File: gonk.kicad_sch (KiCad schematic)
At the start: 10 parts

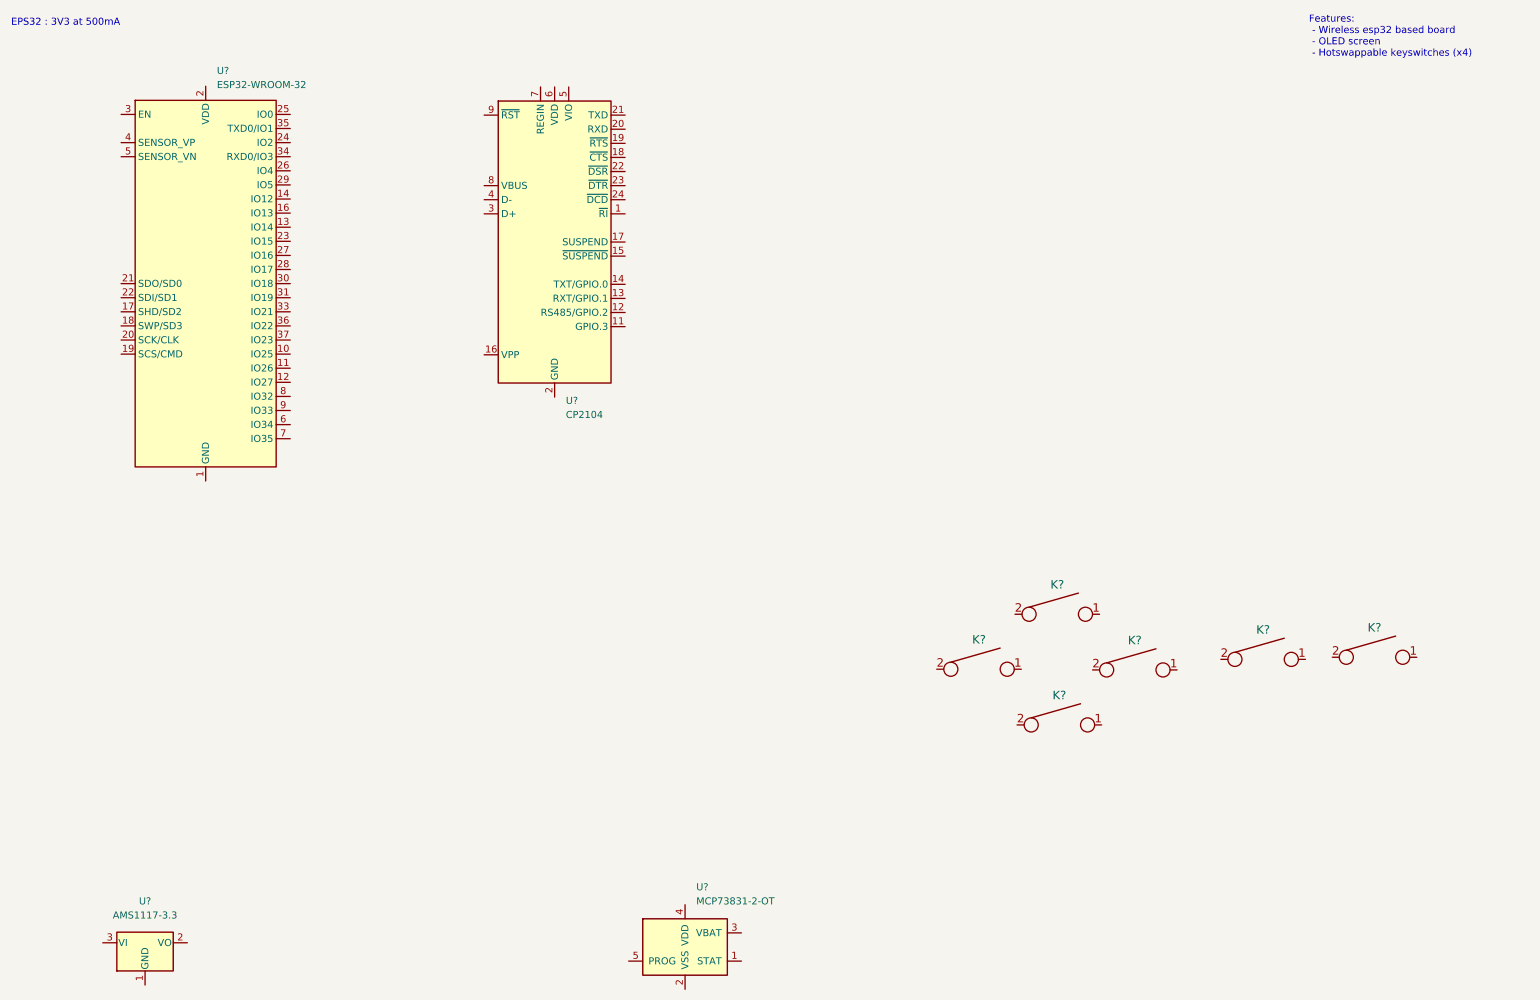
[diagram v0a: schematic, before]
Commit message: Added heiarchical
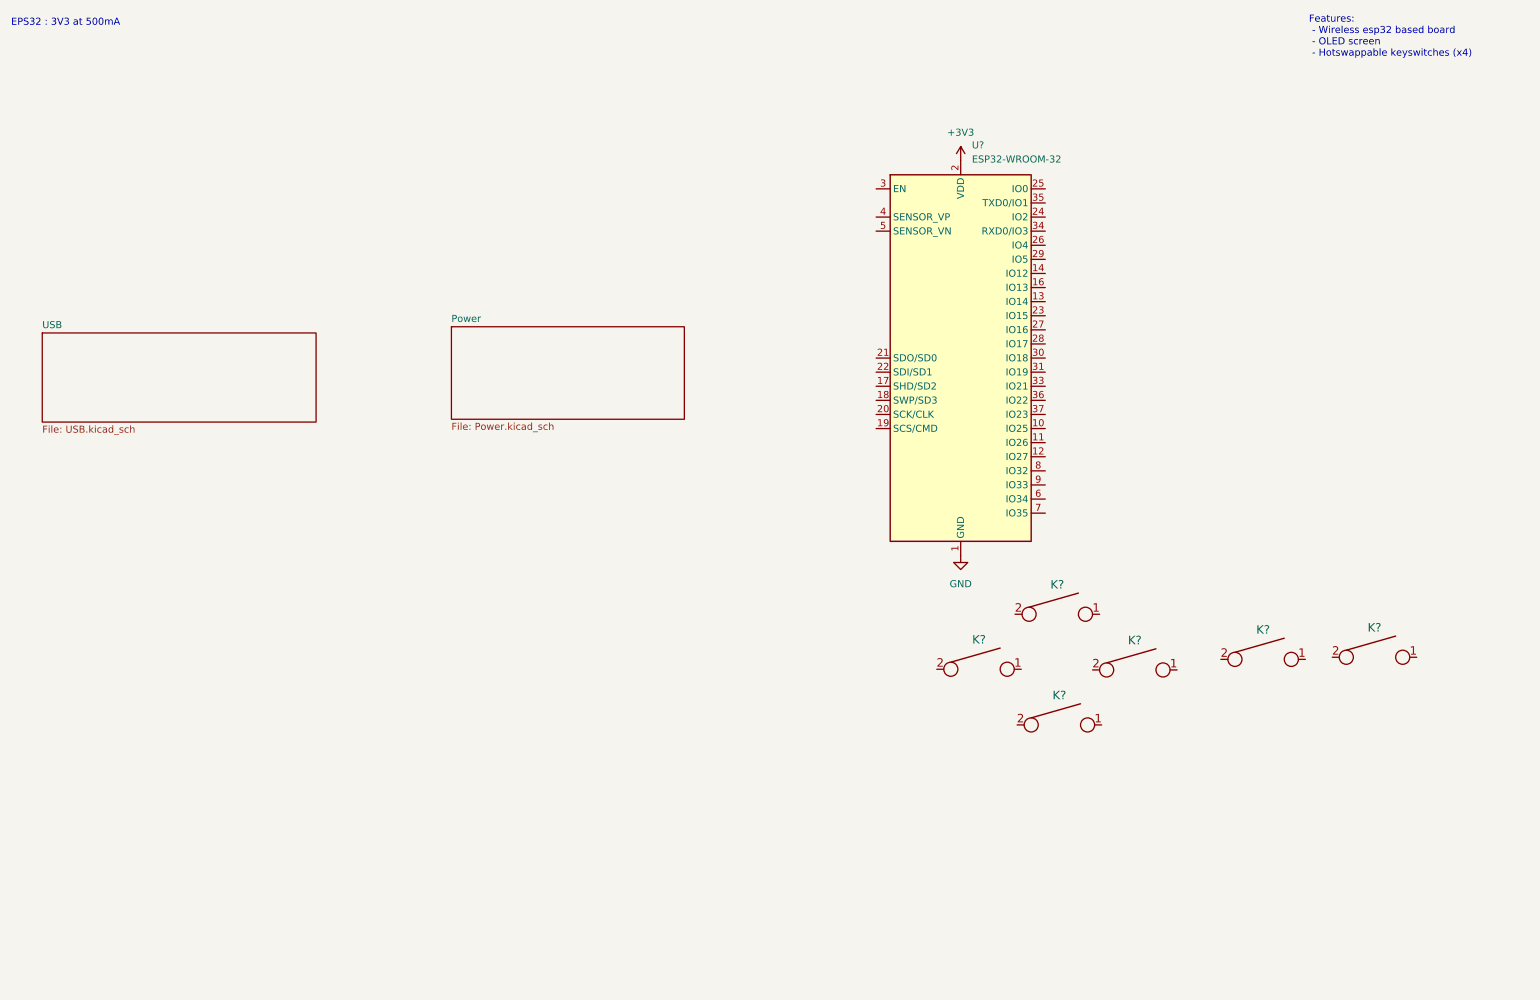
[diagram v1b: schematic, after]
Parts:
- removed U?: CP2104, Package_DFN_QFN:QFN-24-1EP_4x4mm_P0.5mm_EP2.6x2.6mm, symbol Interface_USB:CP2104
- removed U?: AMS1117-3.3, Package_TO_SOT_SMD:SOT-223-3_TabPin2, symbol Regulator_Linear:AMS1117-3.3
- removed U?: MCP73831-2-OT, Package_TO_SOT_SMD:SOT-23-5, symbol Battery_Management:MCP73831-2-OT
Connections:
- net GND: now reaches U?.1 (GND), U?.15 (GND), U?.38 (GND), U?.39 (GND)
- net +3V3: now reaches U?.2 (VDD)
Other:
- added sheet Power (Power.kicad_sch)
- added sheet USB (USB.kicad_sch)
- moved on the sheet: U?
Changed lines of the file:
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@@
     (pin "2")
-  )
-  (symbol (lib_id "Interface_USB:CP2104") (at 112.776 55.245 0) (unit 1)
-    (in_bom yes) (on_board yes) (fields_autoplaced)
-    (property "Reference" "U?" (id 0) (at 114.7954 83.82 0)
-      (effects (font (size 1.27 1.27)) (justify left))
-    )
-    (property "Value" "CP2104" (id 1) (at 114.7954 86.36 0)
-      (effects (font (size 1.27 1.27)) (justify left))
-    )
-    (property "Footprint" "Package_DFN_QFN:QFN-24-1EP_4x4mm_P0.5mm_EP2.6x2.6mm" (id 2) (at 141.986 107.315 0)
-      (effects (font (size 1.27 1.27)) (justify left) hide)
-    )
-    (property "Datasheet" "https://www.silabs.com/documents/public/data-sheets/cp2104.pdf" (id 3) (at 218.186 45.085 0)
-      (effects (font (size 1.27 1.27)) hide)
-    )
-    (pin "1")
-    (pin "10")
-    (pin "11")
-    (pin "12")
-    (pin "13")
-    (pin "14")
-    (pin "15")
-    (pin "16")
-    (pin "17")
-    (pin "18")
-    (pin "19")
-    (pin "2")
-    (pin "20")
-    (pin "21")
-    (pin "22")
-    (pin "23")
-    (pin "24")
-    (pin "25")
-    (pin "3")
-    (pin "4")
-    (pin "5")
-    (pin "6")
-    (pin "7")
-    (pin "8")
-    (pin "9")
   )
   (symbol (lib_id "keyboard_parts:KEYSW") (at 203.708 142.24 0) (unit 1)
@@
     (pin "2")
   )
-  (symbol (lib_id "Regulator_Linear:AMS1117-3.3") (at 38.989 181.483 0) (unit 1)
-    (in_bom yes) (on_board yes) (fields_autoplaced)
-    (property "Reference" "U?" (id 0) (at 38.989 173.99 0))
-    (property "Value" "AMS1117-3.3" (id 1) (at 38.989 176.53 0))
-    (property "Footprint" "Package_TO_SOT_SMD:SOT-223-3_TabPin2" (id 2) (at 38.989 176.403 0)
-      (effects (font (size 1.27 1.27)) hide)
-    )
-    (property "Datasheet" "http://www.advanced-monolithic.com/pdf/ds1117.pdf" (id 3) (at 41.529 187.833 0)
-      (effects (font (size 1.27 1.27)) hide)
-    )
-    (pin "1")
-    (pin "2")
-    (pin "3")
+  (symbol (lib_id "power:+3V3") (at 185.928 40.5892 0) (unit 1)
+    (in_bom yes) (on_board yes) (fields_autoplaced)
+    (property "Reference" "#PWR?" (id 0) (at 185.928 44.3992 0)
+      (effects (font (size 1.27 1.27)) hide)
+    )
+    (property "Value" "+3V3" (id 1) (at 185.928 35.5092 0))
+    (property "Footprint" "" (id 2) (at 185.928 40.5892 0)
+      (effects (font (size 1.27 1.27)) hide)
+    )
+    (property "Datasheet" "" (id 3) (at 185.928 40.5892 0)
+      (effects (font (size 1.27 1.27)) hide)
+    )
+    (pin "1")
+  )
+  (symbol (lib_id "power:GND") (at 185.928 111.7092 0) (unit 1)
+    (in_bom yes) (on_board yes) (fields_autoplaced)
+    (property "Reference" "#PWR?" (id 0) (at 185.928 118.0592 0)
+      (effects (font (size 1.27 1.27)) hide)
+    )
+    (property "Value" "GND" (id 1) (at 185.928 116.84 0))
+    (property "Footprint" "" (id 2) (at 185.928 111.7092 0)
+      (effects (font (size 1.27 1.27)) hide)
+    )
+    (property "Datasheet" "" (id 3) (at 185.928 111.7092 0)
+      (effects (font (size 1.27 1.27)) hide)
+    )
+    (pin "1")
   )
   (symbol (lib_id "keyboard_parts:KEYSW") (at 240.411 130.429 0) (unit 1)
@@
     (pin "2")
   )
-  (symbol (lib_id "Battery_Management:MCP73831-2-OT") (at 136.271 182.245 0) (unit 1)
-    (in_bom yes) (on_board yes) (fields_autoplaced)
-    (property "Reference" "U?" (id 0) (at 138.2904 171.45 0)
+  (symbol (lib_id "RF_Module:ESP32-WROOM-32") (at 185.928 76.1492 0) (unit 1)
+    (in_bom yes) (on_board yes) (fields_autoplaced)
+    (property "Reference" "U?" (id 0) (at 187.9474 37.7952 0)
       (effects (font (size 1.27 1.27)) (justify left))
     )
-    (property "Value" "MCP73831-2-OT" (id 1) (at 138.2904 173.99 0)
+    (property "Value" "ESP32-WROOM-32" (id 1) (at 187.9474 40.3352 0)
       (effects (font (size 1.27 1.27)) (justify left))
     )
-    (property "Footprint" "Package_TO_SOT_SMD:SOT-23-5" (id 2) (at 137.541 188.595 0)
-      (effects (font (size 1.27 1.27) italic) (justify left) hide)
-    )
-    (property "Datasheet" "http://ww1.microchip.com/downloads/en/DeviceDoc/20001984g.pdf" (id 3) (at 132.461 183.515 0)
-      (effects (font (size 1.27 1.27)) hide)
-    )
-    (pin "1")
-    (pin "2")
-    (pin "3")
-    (pin "4")
-    (pin "5")
-  )
-  (symbol (lib_id "RF_Module:ESP32-WROOM-32") (at 49.911 62.738 0) (unit 1)
-    (in_bom yes) (on_board yes) (fields_autoplaced)
-    (property "Reference" "U?" (id 0) (at 51.9304 24.384 0)
-      (effects (font (size 1.27 1.27)) (justify left))
-    )
-    (property "Value" "ESP32-WROOM-32" (id 1) (at 51.9304 26.924 0)
-      (effects (font (size 1.27 1.27)) (justify left))
-    )
-    (property "Footprint" "RF_Module:ESP32-WROOM-32" (id 2) (at 49.911 100.838 0)
-      (effects (font (size 1.27 1.27)) hide)
-    )
-    (property "Datasheet" "https://www.espressif.com/sites/default/files/documentation/esp32-wroom-32_datasheet_en.pdf" (id 3) (at 42.291 61.468 0)
+    (property "Footprint" "RF_Module:ESP32-WROOM-32" (id 2) (at 185.928 114.2492 0)
+      (effects (font (size 1.27 1.27)) hide)
+    )
+    (property "Datasheet" "https://www.espressif.com/sites/default/files/documentation/esp32-wroom-32_datasheet_en.pdf" (id 3) (at 178.308 74.8792 0)
       (effects (font (size 1.27 1.27)) hide)
     )
@@
     (pin "9")
   )
+  (sheet (at 94.1832 70.5104) (size 41.9608 16.6624) (fields_autoplaced)
+    (stroke (width 0.1524) (type solid) (color 0 0 0 0))
+    (fill (color 0 0 0 0.0000))
+    (property "Sheet name" "Power" (id 0) (at 94.1832 69.7988 0)
+      (effects (font (size 1.27 1.27)) (justify left bottom))
+    )
+    (property "Sheet file" "Power.kicad_sch" (id 1) (at 94.1832 87.7574 0)
+      (effects (font (size 1.27 1.27)) (justify left top))
+    )
+  )
+  (sheet (at 20.4724 71.628) (size 49.3268 16.0528) (fields_autoplaced)
+    (stroke (width 0.1524) (type solid) (color 0 0 0 0))
+    (fill (color 0 0 0 0.0000))
+    (property "Sheet name" "USB" (id 0) (at 20.4724 70.9164 0)
+      (effects (font (size 1.27 1.27)) (justify left bottom))
+    )
+    (property "Sheet file" "USB.kicad_sch" (id 1) (at 20.4724 88.2654 0)
+      (effects (font (size 1.27 1.27)) (justify left top))
+    )
+  )
   (sheet_instances
     (path "/" (page "1"))
+    (path "/ebb9ad05-07ec-437e-88a4-85793ff36bdf" (page "2"))
+    (path "/207b395a-56be-41f1-8a18-a435f59fa0c1" (page "3"))
   )
   (symbol_instances
+    (path "/63ce052f-fc52-47ca-8062-80e6d0e6fddd"
+      (reference "#PWR?") (unit 1) (value "+3V3") (footprint "")
+    )
+    (path "/96325eac-771c-4c16-ba14-694dd24fa9e5"
+      (reference "#PWR?") (unit 1) (value "GND") (footprint "")
+    )
+    (path "/207b395a-56be-41f1-8a18-a435f59fa0c1/62565191-2860-4e92-b159-c8999a425102"
+      (reference "C?") (unit 1) (value "C_Small") (footprint "")
+    )
+    (path "/207b395a-56be-41f1-8a18-a435f59fa0c1/b0a4ac5d-73d5-4d08-92ca-65537b93710d"
+      (reference "C?") (unit 1) (value "C_Small") (footprint "")
+    )
     (path "/0dff86f1-14a4-4917-9b26-3f249b593c6a"
       (reference "K?") (unit 1) (value "KEYSW") (footprint "")
@@
       (reference "K?") (unit 1) (value "KEYSW") (footprint "")
     )
-    (path "/2ed147f7-08e6-4a24-8be2-f9052e8c0ea6"
+    (path "/ebb9ad05-07ec-437e-88a4-85793ff36bdf/240a430e-ca62-4703-ae6d-dfba837b677f"
+      (reference "P?") (unit 1) (value "USB_C_Plug") (footprint "")
+    )
+    (path "/207b395a-56be-41f1-8a18-a435f59fa0c1/540f716a-9e64-4c0f-a302-ad4487be86f4"
+      (reference "U?") (unit 1) (value "MCP73831-2-OT") (footprint "Package_TO_SOT_SMD:SOT-23-5")
+    )
+    (path "/ebb9ad05-07ec-437e-88a4-85793ff36bdf/9162a1fb-3573-4860-9273-2231d802b470"
       (reference "U?") (unit 1) (value "CP2104") (footprint "Package_DFN_QFN:QFN-24-1EP_4x4mm_P0.5mm_EP2.6x2.6mm")
     )
-    (path "/780634cc-ca09-452d-826e-c191070c15f8"
+    (path "/207b395a-56be-41f1-8a18-a435f59fa0c1/b876f5bf-ac52-487e-8467-c3fea9a4dc29"
       (reference "U?") (unit 1) (value "AMS1117-3.3") (footprint "Package_TO_SOT_SMD:SOT-223-3_TabPin2")
     )
-    (path "/b2e41db8-5861-439d-9d94-021ed293689f"
-      (reference "U?") (unit 1) (value "MCP73831-2-OT") (footprint "Package_TO_SOT_SMD:SOT-23-5")
-    )
     (path "/ceeb9c53-3901-4d0a-9ec7-48a467f1f324"
